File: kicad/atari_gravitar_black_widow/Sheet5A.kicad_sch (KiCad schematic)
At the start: 121 parts, among them Q2 2N6044, Q3 2N6044, Q4 2N6044

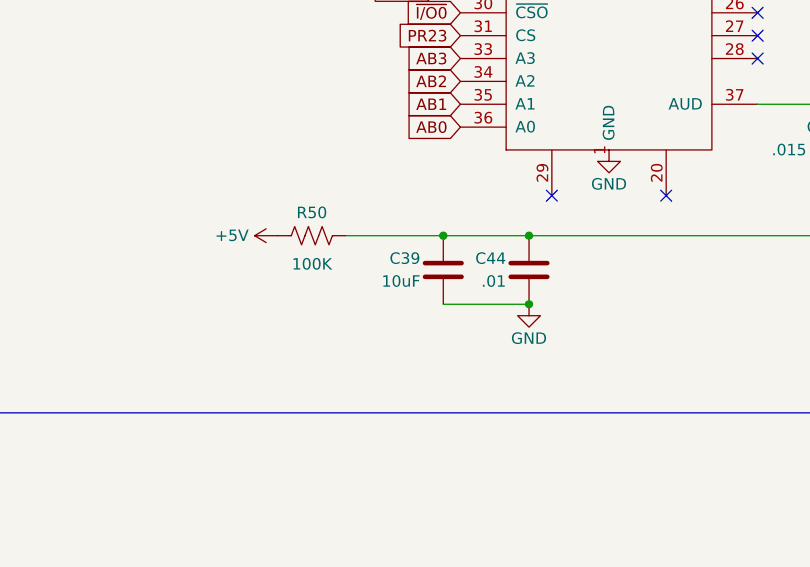
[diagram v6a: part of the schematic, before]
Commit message: caps polarity, c39, c38, transistors holes to .125 mil
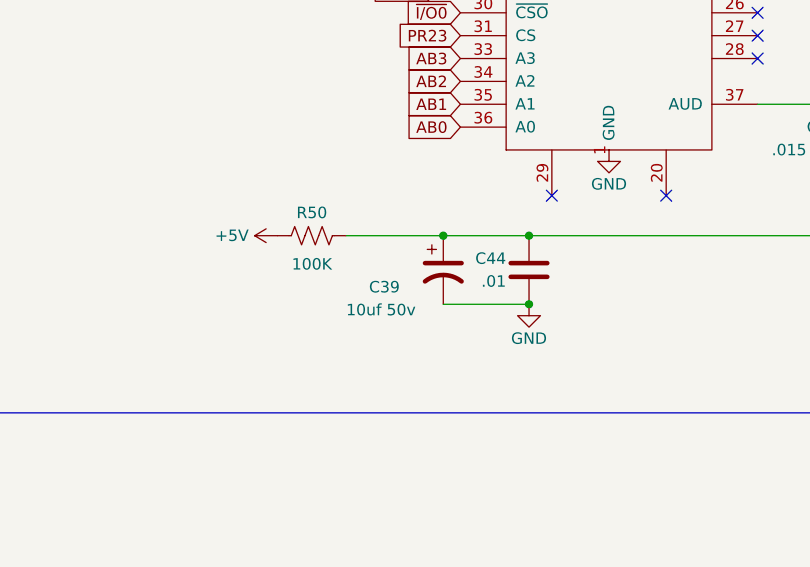
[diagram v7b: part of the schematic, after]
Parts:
- removed C39: 10uF, Star_Wars_Vector_PCB:CapElec2, symbol Device:C
- added C39: 10uf 50v, Star_Wars_Vector_PCB:CapElec2, symbol Device:C_Polarized_US
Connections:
- net GND: now also C39.2
- net at B_5.5 (+), C44.2, D_5.10 (+)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: now also C39.1
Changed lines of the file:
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@@
   (junction (at 499.745 117.475) (diameter 0) (color 0 0 0 0)
   )
+  (junction (at 339.725 186.69) (diameter 0) (color 0 0 0 0)
+  )
   (junction (at 92.71 114.3) (diameter 0) (color 0 0 0 0)
   )
@@
   (junction (at 125.73 130.81) (diameter 0) (color 0 0 0 0)
   )
-  (junction (at 339.725 186.69) (diameter 0) (color 0 0 0 0)
-  )
   (junction (at 327.66 145.415) (diameter 0) (color 0 0 0 0)
   )
@@
     (stroke (width 0) (type default) (color 0 0 0 0))
   )
-  (wire (pts (xy 339.725 186.69) (xy 349.25 186.69))
+  (wire (pts (xy 328.93 186.69) (xy 339.725 186.69))
     (stroke (width 0) (type default) (color 0 0 0 0))
   )
@@
     (stroke (width 0) (type default) (color 0 0 0 0))
   )
+  (wire (pts (xy 339.725 186.69) (xy 349.25 186.69))
+    (stroke (width 0) (type default) (color 0 0 0 0))
+  )
   (wire (pts (xy 66.675 297.18) (xy 139.7 297.18))
     (stroke (width 0) (type default) (color 0 0 0 0))
@@
     (stroke (width 0) (type default) (color 0 0 0 0))
   )
-  (wire (pts (xy 328.93 186.69) (xy 339.725 186.69))
-    (stroke (width 0) (type default) (color 0 0 0 0))
-  )
   (wire (pts (xy 279.4 142.875) (xy 276.225 142.875))
     (stroke (width 0) (type default) (color 0 0 0 0))
@@
     (pin "2")
   )
-  (symbol (lib_id "Device:C") (at 339.725 190.5 180) (unit 1)
-    (in_bom yes) (on_board yes)
-    (property "Reference" "C39" (id 0) (at 337.185 189.23 0)
-      (effects (font (size 1.27 1.27)) (justify left))
-    )
-    (property "Value" "10uF" (id 1) (at 337.185 191.77 0)
-      (effects (font (size 1.27 1.27)) (justify left))
-    )
-    (property "Footprint" "Star_Wars_Vector_PCB:CapElec2" (id 2) (at 338.7598 186.69 0)
-      (effects (font (size 1.27 1.27)) hide)
-    )
-    (property "Datasheet" "~" (id 3) (at 339.725 190.5 0)
-      (effects (font (size 1.27 1.27)) hide)
-    )
-    (pin "1")
-    (pin "2")
-  )
   (symbol (lib_id "Device:R_US") (at 347.98 290.83 270) (unit 1)
     (in_bom yes) (on_board yes)
@@
     (pin "1")
   )
+  (symbol (lib_id "Device:C_Polarized_US") (at 339.725 190.5 0) (unit 1)
+    (in_bom yes) (on_board yes)
+    (property "Reference" "C39" (id 0) (at 331.47 192.405 0)
+      (effects (font (size 1.27 1.27)) (justify left))
+    )
+    (property "Value" "10uf 50v" (id 1) (at 328.93 194.945 0)
+      (effects (font (size 1.27 1.27)) (justify left))
+    )
+    (property "Footprint" "Star_Wars_Vector_PCB:CapElec2" (id 2) (at 339.725 190.5 0)
+      (effects (font (size 1.27 1.27)) hide)
+    )
+    (property "Datasheet" "~" (id 3) (at 339.725 190.5 0)
+      (effects (font (size 1.27 1.27)) hide)
+    )
+    (pin "1")
+    (pin "2")
+  )
   (symbol (lib_id "Device:R_US") (at 92.71 231.14 0) (mirror x) (unit 1)

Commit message: Fixed C34 and 6MHZ trace
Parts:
- C34: footprint Star_Wars_Vector_PCB:CapYellow -> Star_Wars_Vector_PCB:GenericComp
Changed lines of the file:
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@@
       (effects (font (size 1.27 1.27)) (justify left))
     )
-    (property "Footprint" "Star_Wars_Vector_PCB:CapYellow" (id 2) (at 417.83 151.4348 0)
+    (property "Footprint" "Star_Wars_Vector_PCB:GenericComp" (id 2) (at 417.83 151.4348 0)
       (effects (font (size 1.27 1.27)) hide)
     )
